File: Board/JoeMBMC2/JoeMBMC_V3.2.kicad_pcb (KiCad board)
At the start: 2 copper layers, 68 x 92 mm, 70 parts, among them J1 5007620481, J2 CAN2_T, J3 CAN1_T, Q1 BSO615NG, Q2 BSO615NG, Q3 P-Chanel Mosfet, U1 Teensy4.0, U2 SN65HVD230, U3 DCDC 5V, U4 IS281-4, U5 SN65HVD230, U6 DCDC 3.3V, U7 Level Shifter 5V to 3V, U8 Level Shifter 5V to 3V

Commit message: Board redesign
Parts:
- moved C2 2.25 mm to (161.3, 59.0)
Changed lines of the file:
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@@
   )
   (footprint "Capacitor_SMD:C_0805_2012Metric" (layer "F.Cu")
-    (at 161.33 56.7 90)
+    (at 161.3 58.95 90)
     (descr "Capacitor SMD 0805 (2012 Metric), square (rectangular) end terminal, IPC_7351 nominal, (Body size source: IPC-SM-782 page 76, https://www.pcb-3d.com/wordpress/wp-content/uploads/ipc-sm-782a_amendment_1_and_2.pdf, https://docs.google.com/spreadsheets/d/1BsfQQcO9C6DZCsRaXUlFlo91Tg2WpOkGARC1WS5S8t0/edit?usp=sharing), generated with kicad-footprint-generator")
     (tags "capacitor")
@@
   (segment (start 145.3525 90.7325) (end 145.48 90.605) (width 0.25) (layer "B.Cu") (net 18))
   (segment (start 135.508884 92.025) (end 134.114974 90.63109) (width 0.25) (layer "B.Cu") (net 18))
-  (segment (start 134.114974 90.65) (end 134.114974 90.63109) (width 0.25) (layer "B.Cu") (net 18))
   (segment (start 144.090475 92.025) (end 135.508884 92.025) (width 0.25) (layer "B.Cu") (net 18))
   (segment (start 131.483884 88) (end 128.93 88) (width 0.25) (layer "B.Cu") (net 18))
@@
   (segment (start 124.4975 55.5475) (end 123.14 54.19) (width 0.25) (layer "F.Cu") (net 61))
   (segment (start 143.56 63.06) (end 137.4125 63.06) (width 0.25) (layer "F.Cu") (net 61))
-  (segment (start 135.6 64.5) (end 130.4852 59.3852) (width 0.25) (layer "F.Cu") (net 63))
   (segment (start 130.4852 59.3852) (end 127.292465 59.3852) (width 0.25) (layer "F.Cu") (net 63))
-  (segment (start 158.8 65.6) (end 157.7 64.5) (width 0.25) (layer "F.Cu") (net 63))
-  (segment (start 157.7 64.5) (end 135.6 64.5) (width 0.25) (layer "F.Cu") (net 63))
+  (segment (start 135.675 64.575) (end 130.4852 59.3852) (width 0.25) (layer "F.Cu") (net 63))
+  (segment (start 158.8 65.6) (end 157.775 64.575) (width 0.25) (layer "F.Cu") (net 63))
+  (segment (start 157.775 64.575) (end 135.675 64.575) (width 0.25) (layer "F.Cu") (net 63))
   (segment (start 156.98 77.355) (end 156.98 78.705) (width 0.25) (layer "F.Cu") (net 64))
   (via (at 156.98 78.705) (size 0.8) (drill 0.4) (layers "F.Cu" "B.Cu") (free) (net 64))
@@
         (xy 135.884 122.4)
         (xy 162.264 122.4)
-        (xy 162.264 56.9)
-        (xy 157.035 56.9)
+        (xy 162.264 59.1)
+        (xy 157.035 59.1)
         (xy 157.035 48.26)
         (xy 108.585 48.26)

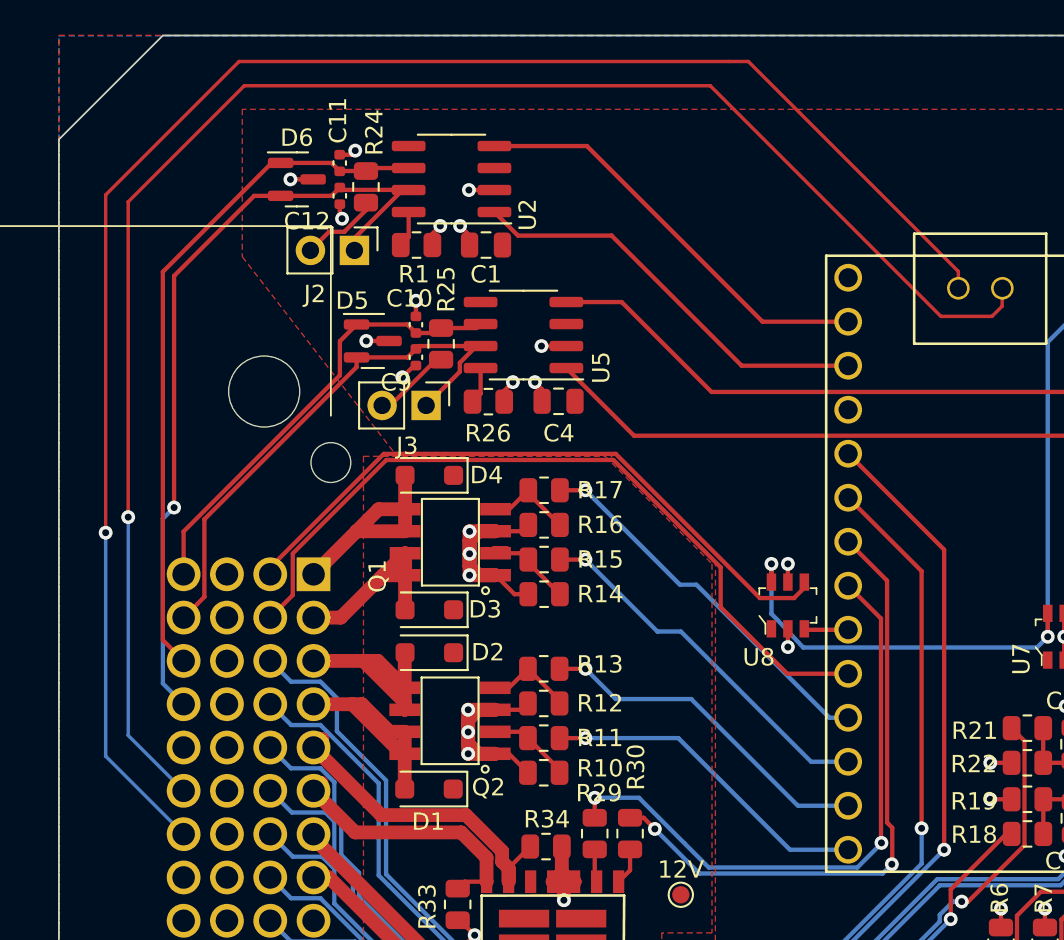
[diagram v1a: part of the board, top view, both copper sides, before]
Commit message: USB traces closer together
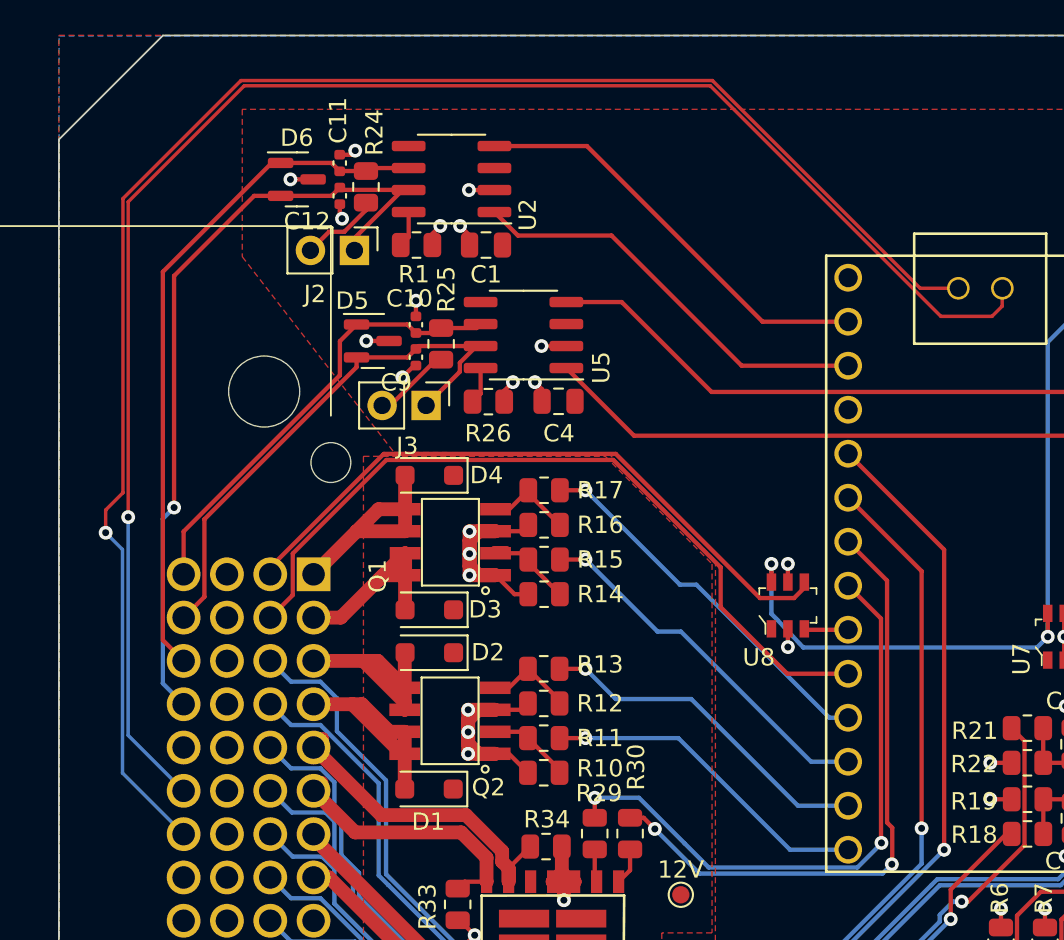
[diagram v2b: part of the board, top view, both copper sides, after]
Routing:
- net Teensy_D+: track 97.2 -> 95.0 mm
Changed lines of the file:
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@@
   (segment (start 130.97 92.185) (end 130.31 92.845) (width 0.25) (layer "F.Cu") (net 54))
   (segment (start 130.97 90.98) (end 130.97 92.185) (width 0.25) (layer "F.Cu") (net 54))
-  (segment (start 136.7 45.5) (end 108.4 45.5) (width 0.2) (layer "F.Cu") (net 55))
-  (segment (start 149.92 57.62) (end 137.8 45.5) (width 0.2) (layer "F.Cu") (net 55))
-  (segment (start 100.7 53.2) (end 100.7 72.7) (width 0.2) (layer "F.Cu") (net 55))
-  (segment (start 137.8 45.5) (end 136.7 45.5) (width 0.2) (layer "F.Cu") (net 55))
-  (segment (start 149.92 58.59) (end 149.92 57.62) (width 0.2) (layer "F.Cu") (net 55))
-  (segment (start 108.4 45.5) (end 100.7 53.2) (width 0.2) (layer "F.Cu") (net 55))
+  (segment (start 135.724264 46.6) (end 147.714264 58.59) (width 0.2) (layer "F.Cu") (net 55))
+  (segment (start 147.714264 58.59) (end 149.92 58.59) (width 0.2) (layer "F.Cu") (net 55))
+  (segment (start 108.51 46.6) (end 135.724264 46.6) (width 0.2) (layer "F.Cu") (net 55))
+  (segment (start 100.7 71.39) (end 101.7 70.39) (width 0.2) (layer "F.Cu") (net 55))
+  (segment (start 101.7 70.39) (end 101.7 53.41) (width 0.2) (layer "F.Cu") (net 55))
+  (segment (start 101.7 53.41) (end 108.51 46.6) (width 0.2) (layer "F.Cu") (net 55))
+  (segment (start 100.7 72.7) (end 100.7 71.39) (width 0.2) (layer "F.Cu") (net 55))
   (via (at 100.7 72.7) (size 0.8) (drill 0.4) (layers "F.Cu" "B.Cu") (net 55))
-  (segment (start 100.7 85.6) (end 100.7 72.7) (width 0.2) (layer "B.Cu") (net 55))
-  (segment (start 105.2 90.1) (end 100.7 85.6) (width 0.2) (layer "B.Cu") (net 55))
+  (segment (start 101.67 86.57) (end 101.67 73.67) (width 0.2) (layer "B.Cu") (net 55))
+  (segment (start 101.67 73.67) (end 100.7 72.7) (width 0.2) (layer "B.Cu") (net 55))
+  (segment (start 105.2 90.1) (end 101.67 86.57) (width 0.2) (layer "B.Cu") (net 55))
   (segment (start 135.6 46.9) (end 108.7 46.9) (width 0.2) (layer "F.Cu") (net 56))
   (segment (start 102 53.6) (end 102 71.8) (width 0.2) (layer "F.Cu") (net 56))

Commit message: Board Updates
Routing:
- net Teensy_D-: track 95.4 -> 94.1 mm
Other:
- board text added: "JoeMBMC V3.2.1"
- board text removed: "JoeMBMC V3.2"
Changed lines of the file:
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@@
   (gr_line (start 104 44) (end 166 44)
     (stroke (width 0.1) (type solid)) (layer "Edge.Cuts"))
-  (gr_text "JoeMBMC V3.2" (at 153 133.81) (layer "B.SilkS")
+  (gr_text "JoeMBMC V3.2.1" (at 153 133.81) (layer "B.SilkS")
     (effects (font (size 2 2) (thickness 0.15)) (justify mirror))
   )
@@
   (segment (start 112.7 90.325293) (end 112.7 90.1) (width 0.8) (layer "F.Cu") (net 44))
   (segment (start 120.944707 98.57) (end 112.7 90.325293) (width 0.8) (layer "F.Cu") (net 44))
-  (segment (start 122.69 98.535) (end 121.055 98.535) (width 0.25) (layer "F.Cu") (net 44))
+  (segment (start 122.69 98.535) (end 121.055 98.535) (width 0.8) (layer "F.Cu") (net 44))
   (segment (start 121.055 98.535) (end 121.02 98.57) (width 0.8) (layer "F.Cu") (net 44))
   (segment (start 121.02 98.57) (end 120.944707 98.57) (width 0.8) (layer "F.Cu") (net 44))
@@
   (segment (start 101.67 73.67) (end 100.7 72.7) (width 0.2) (layer "B.Cu") (net 55))
   (segment (start 105.2 90.1) (end 101.67 86.57) (width 0.2) (layer "B.Cu") (net 55))
+  (segment (start 151.608 59.442) (end 152.46 58.59) (width 0.2) (layer "F.Cu") (net 56))
+  (segment (start 147.635 58.935) (end 148.142 59.442) (width 0.2) (layer "F.Cu") (net 56))
   (segment (start 135.6 46.9) (end 108.7 46.9) (width 0.2) (layer "F.Cu") (net 56))
   (segment (start 102 53.6) (end 102 71.8) (width 0.2) (layer "F.Cu") (net 56))
-  (segment (start 152.45 58.53) (end 152.45 59.625) (width 0.2) (layer "F.Cu") (net 56))
+  (segment (start 148.142 59.442) (end 151.608 59.442) (width 0.2) (layer "F.Cu") (net 56))
+  (segment (start 147.635 58.935) (end 135.6 46.9) (width 0.2) (layer "F.Cu") (net 56))
   (segment (start 108.7 46.9) (end 102 53.6) (width 0.2) (layer "F.Cu") (net 56))
-  (segment (start 148.9125 60.2125) (end 135.6 46.9) (width 0.2) (layer "F.Cu") (net 56))
-  (segment (start 151.8625 60.2125) (end 148.9125 60.2125) (width 0.2) (layer "F.Cu") (net 56))
-  (segment (start 152.45 59.625) (end 151.8625 60.2125) (width 0.2) (layer "F.Cu") (net 56))
   (via (at 102 71.8) (size 0.8) (drill 0.4) (layers "F.Cu" "B.Cu") (net 56))
   (segment (start 102 84.4) (end 102 71.8) (width 0.2) (layer "B.Cu") (net 56))
